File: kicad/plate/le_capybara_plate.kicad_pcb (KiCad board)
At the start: 2 copper layers, 231.6 x 92.5 mm, 34 parts, among them SW1 EC_SW, SW10 EC_SW, SW11 EC_SW, SW12 EC_SW, SW13 EC_SW, SW14 EC_SW, SW15 EC_SW, SW16 EC_SW, SW17 EC_SW, SW18 EC_SW, SW19 EC_SW, SW2 EC_SW, SW20 EC_SW, SW21 EC_SW, SW22 EC_SW, SW23 EC_SW, SW24 EC_SW, SW25 EC_SW, SW26 EC_SW, SW27 EC_SW, SW28 EC_SW, SW29 EC_SW, SW3 EC_SW, SW30 EC_SW, SW31 EC_SW, SW32 EC_SW, SW33 EC_SW, SW34 EC_SW, SW4 EC_SW, SW5 EC_SW, SW6 EC_SW, SW7 EC_SW, SW8 EC_SW, SW9 EC_SW

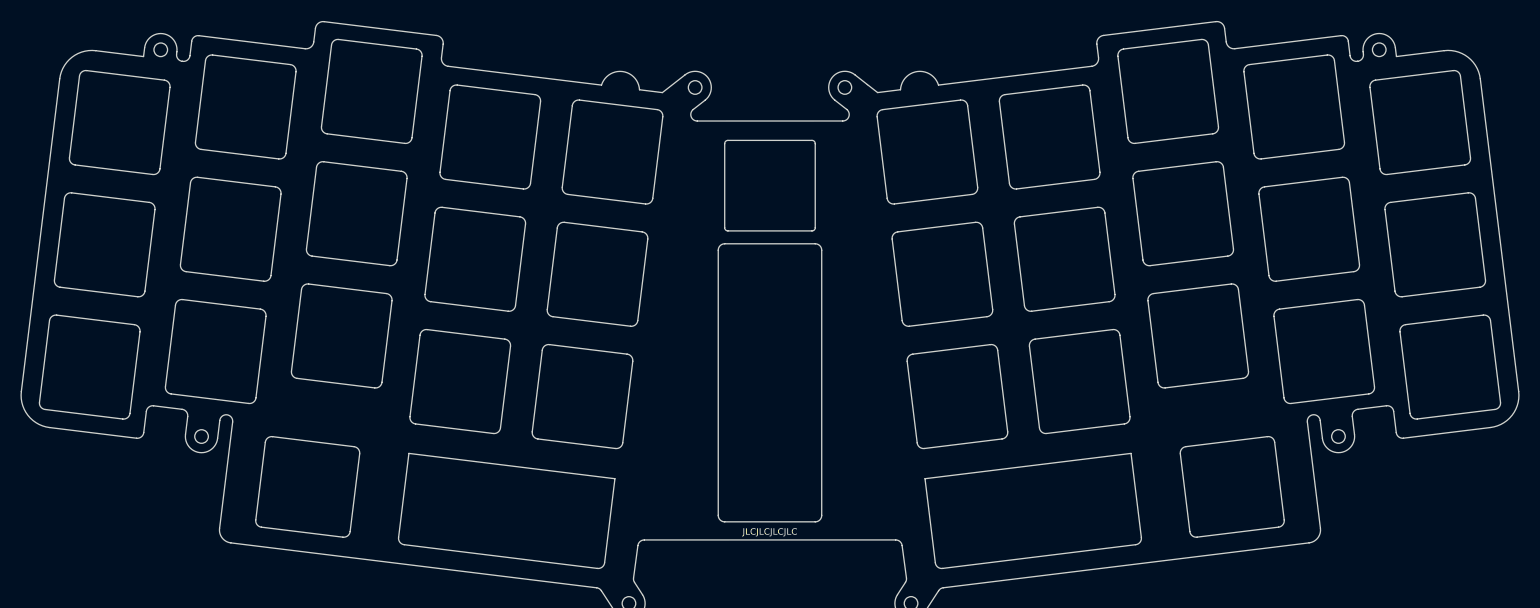
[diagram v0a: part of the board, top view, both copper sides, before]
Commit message: schematic fix and plate tolerance fix
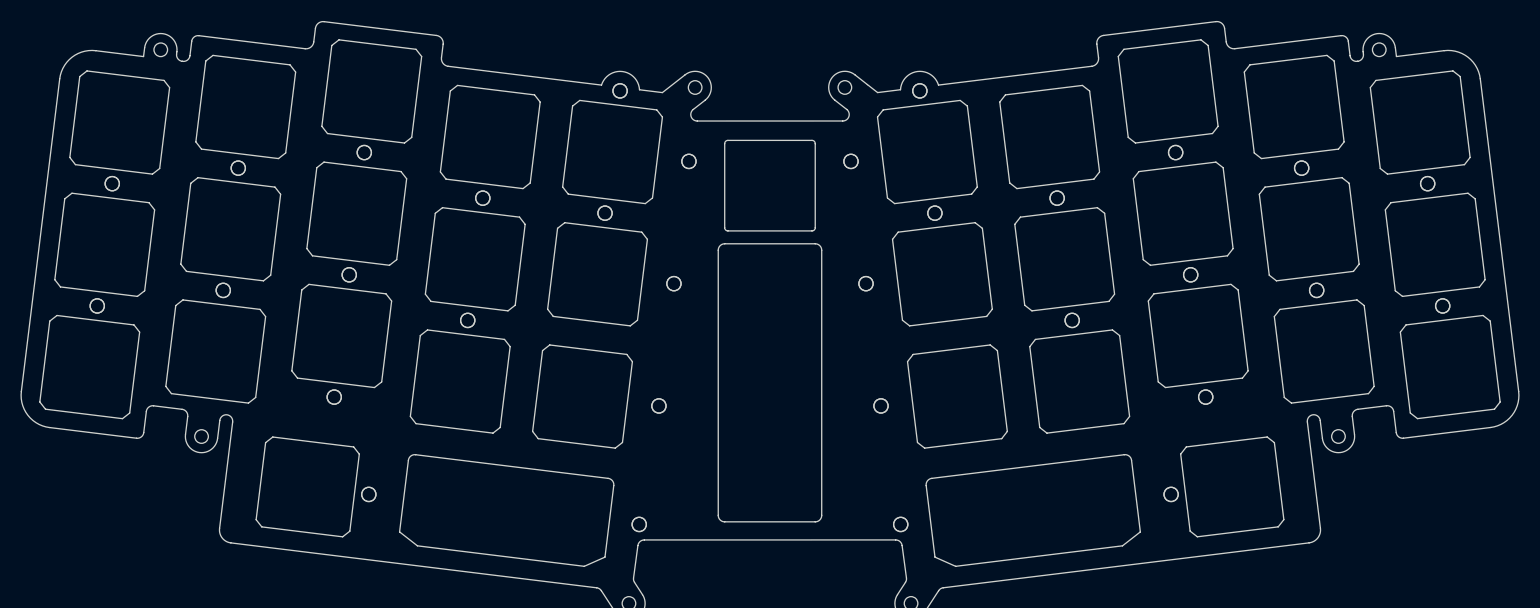
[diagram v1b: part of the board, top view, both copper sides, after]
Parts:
- added H1: M2 Hole, capacitive_sensors:MountingHole_2.2mm_M2, F.Cu at (44.9, 84.1)
- added H10: M2 Hole, capacitive_sensors:MountingHole_2.2mm_M2, F.Cu at (79.3, 117.1)
- added H11: M2 Hole, capacitive_sensors:MountingHole_2.2mm_M2, F.Cu at (161.5, 99.5)
- added H12: M2 Hole, capacitive_sensors:MountingHole_2.2mm_M2, F.Cu at (214.0, 117.1)
- added H13: M2 Hole, capacitive_sensors:MountingHole_2.2mm_M2, F.Cu at (123.5, 69.7)
- added H14: M2 Hole, capacitive_sensors:MountingHole_2.2mm_M2, F.Cu at (129.5, 118.4)
- added H15: M2 Hole, capacitive_sensors:MountingHole_2.2mm_M2, F.Cu at (193.4, 105.2)
- added H16: M2 Hole, capacitive_sensors:MountingHole_2.2mm_M2, F.Cu at (64.4, 81.6)
- added H17: M2 Hole, capacitive_sensors:MountingHole_2.2mm_M2, F.Cu at (62.1, 100.6)
- added H18: M2 Hole, capacitive_sensors:MountingHole_2.2mm_M2, F.Cu at (102.2, 86.3)
- added H19: M2 Hole, capacitive_sensors:MountingHole_2.2mm_M2, F.Cu at (228.9, 81.6)
- added H2: M2 Hole, capacitive_sensors:MountingHole_2.2mm_M2, F.Cu at (126.4, 136.8)
- added H20: M2 Hole, capacitive_sensors:MountingHole_2.2mm_M2, F.Cu at (191.0, 86.3)
- added H21: M2 Hole, capacitive_sensors:MountingHole_2.2mm_M2, F.Cu at (134.1, 80.6)
- added H22: M2 Hole, capacitive_sensors:MountingHole_2.2mm_M2, F.Cu at (84.6, 132.1)
- added H23: M2 Hole, capacitive_sensors:MountingHole_2.2mm_M2, F.Cu at (163.8, 118.4)
- added H24: M2 Hole, capacitive_sensors:MountingHole_2.2mm_M2, F.Cu at (81.6, 98.1)
- added H25: M2 Hole, capacitive_sensors:MountingHole_2.2mm_M2, F.Cu at (99.9, 105.2)
- added H26: M2 Hole, capacitive_sensors:MountingHole_2.2mm_M2, F.Cu at (121.1, 88.6)
- added H27: M2 Hole, capacitive_sensors:MountingHole_2.2mm_M2, F.Cu at (166.9, 136.8)
- added H28: M2 Hole, capacitive_sensors:MountingHole_2.2mm_M2, F.Cu at (211.7, 98.1)
- added H29: M2 Hole, capacitive_sensors:MountingHole_2.2mm_M2, F.Cu at (248.4, 84.1)
- added H3: M2 Hole, capacitive_sensors:MountingHole_2.2mm_M2, F.Cu at (159.2, 80.6)
- added H30: M2 Hole, capacitive_sensors:MountingHole_2.2mm_M2, F.Cu at (209.4, 79.2)
- added H32: M2 Hole, capacitive_sensors:MountingHole_2.2mm_M2, F.Cu at (208.7, 132.1)
- added H33: M2 Hole, capacitive_sensors:MountingHole_2.2mm_M2, F.Cu at (231.2, 100.6)
- added H34: M2 Hole, capacitive_sensors:MountingHole_2.2mm_M2, F.Cu at (250.7, 103.0)
- added H4: M2 Hole, capacitive_sensors:MountingHole_2.2mm_M2, F.Cu at (83.9, 79.2)
- added H5: M2 Hole, capacitive_sensors:MountingHole_2.2mm_M2, F.Cu at (169.8, 69.7)
- added H6: M2 Hole, capacitive_sensors:MountingHole_2.2mm_M2, F.Cu at (131.8, 99.5)
- added H7: M2 Hole, capacitive_sensors:MountingHole_2.2mm_M2, F.Cu at (42.6, 103.0)
- added H9: M2 Hole, capacitive_sensors:MountingHole_2.2mm_M2, F.Cu at (172.1, 88.6)
- SW1, SW10, SW11, SW12, SW13, SW14, SW15, SW16, SW17, SW18, SW19, SW2, SW20, SW21, SW22, SW23, SW24, SW25, SW26, SW27, SW28, SW29, SW3, SW30, SW31, SW34, SW4, SW5, SW6, SW7, SW8, SW9: footprint capacitive_sensors:ec_plate_cutout_topre_14.1x14.7mm -> capacitive_sensors:plate_cut_1U_topre
- SW32, SW33: footprint capacitive_sensors:ec_plate_cutout_topre_2u -> capacitive_sensors:plate_cut_2U_topre
